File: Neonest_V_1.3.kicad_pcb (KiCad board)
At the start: 2 copper layers, 75 x 88 mm, 98 parts, among them J1 Battery Input, J10 Conn_01x02, J11 Conn_01x02, J12 Conn_01x02, J2 Charger Input, J3 693071010811, J4 Conn_01x03, J5 Conn_01x02, J6 Conn_01x05, J7 Conn_01x03, J8 Conn_01x04, J9 Heating pad, Q1 BC817, Q2 BC817, Q3 STB33N65M2, Q4 BC817, Q5 STB33N65M2, Q6 STB33N65M2, Q7 BC817, U1 LM2596T-5, U2 LM1117-3.3, U3 STM32F103CBTx, Y1 32.678kHz, Y2 8Mhz

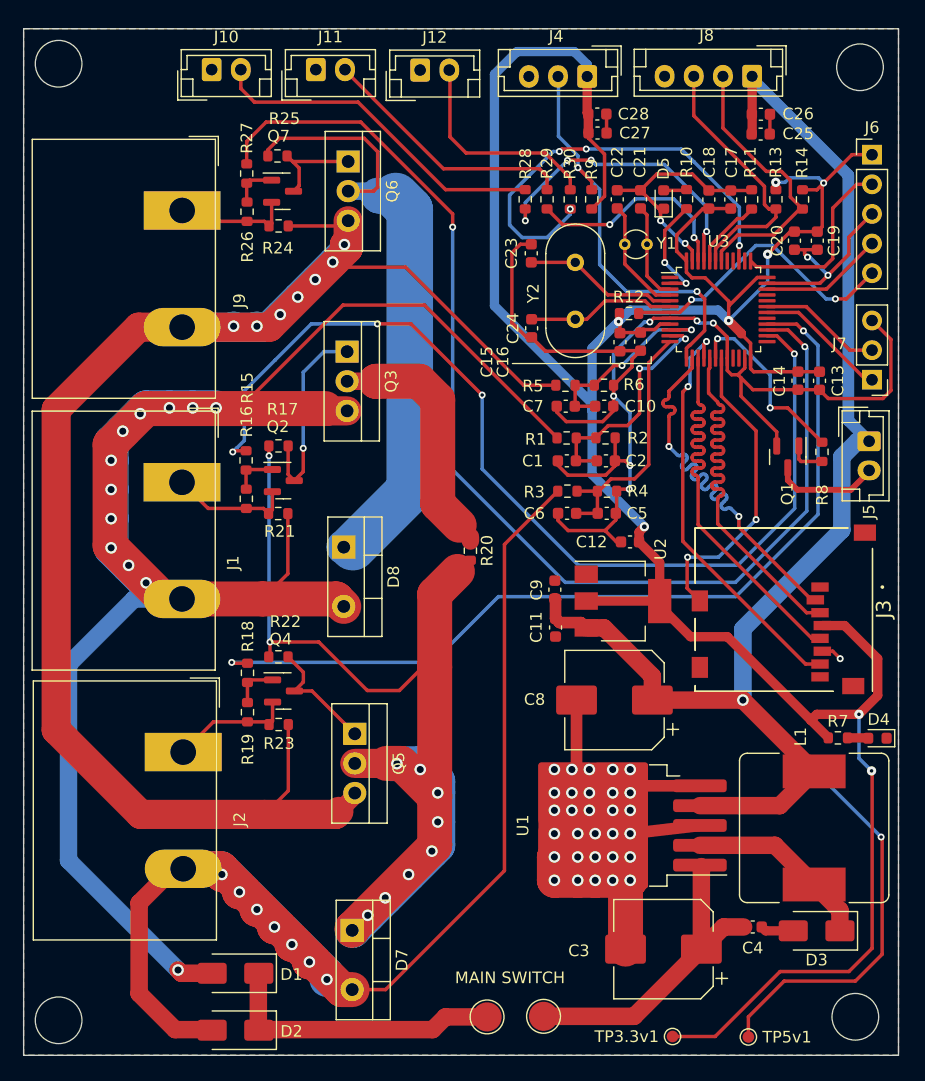
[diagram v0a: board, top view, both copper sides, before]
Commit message: updated silkscreen information
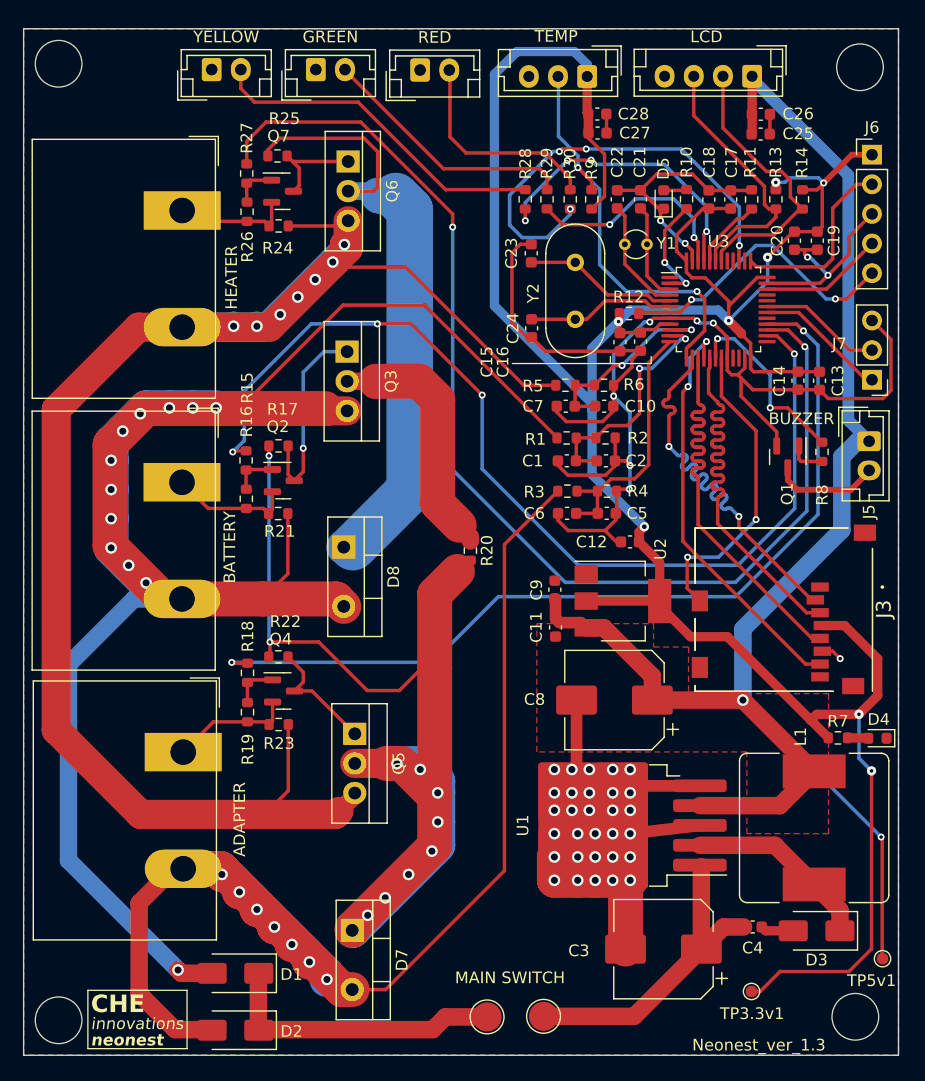
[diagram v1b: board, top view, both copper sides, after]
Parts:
- added REF**: neonest_logo, neonest_logo:neonest_logo, F.Cu at (111.8, 136.4)
- moved TP5v1 13.3 mm to (179.6, 130.7)
- moved TP3.3v1 7.79 mm to (168.4, 133.5)
- renumbered J2 to ADAPTER, J1 to BATTERY, J11 to GREEN, J9 to HEATER, J8 to LCD, J12 to RED, J4 to TEMP, J10 to YELLOW
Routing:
- net +5V: track 151.4 -> 136.4 mm
- net +3V3: track 241.2 -> 232.6 mm
- added copper zone on F.Cu, net +5V
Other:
- board text added: "3.3v"
- board text added: "BUZZER"
- board text added: "Neonest_ver_1.3"
- board text added: "gnd"
- board text added: "nrst"
- board text added: "swclk"
- board text added: "swdio"
